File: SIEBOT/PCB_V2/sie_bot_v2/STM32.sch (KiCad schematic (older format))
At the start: 50 parts, among them P11 CONN_3X2, P12 CONN_3X2, P13 CONN_3X2, P14 CONN_3X2, P8 CONN_12X2, P9 CONN_12X2, Q2 BS170F, Q3 BS170F, Q4 BS170F, Q5 BS170F, Q6 BS170F, Q7 BS170F, Q8 BS170F, Q9 BS170F, U10 STM32F105RC, U11 LT1117CST-3.3, U12 ZXMHC3F381N8, U13 ZXMHC3F381N8, U14 ZXMHC3F381N8, U15 ZXMHC3F381N8, X3 8MHz

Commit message: Ruteo de 3 puentes H, se elimina uno por falta de espacio
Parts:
- removed P14: CONN_3X2, pin_array_3x2, symbol CONN_3X2
- removed Q8, Q9: BS170F, BS170F, symbol MOSFET_N_OPENDOUS
- removed R42, R43: 2.2k, SM0603, symbol R
- removed U15: ZXMHC3F381N8, -SO8, symbol ZXMHC3F381N8
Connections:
- net labels removed: C1M4, C2M4, GMTR4, M41, M42, VMTR4
- wire segments 260 -> 236
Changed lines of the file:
@@
-EESchema Schematic File Version 2  date Sun 02 Oct 2011 08:48:42 PM COT
+EESchema Schematic File Version 2  date Mon 03 Oct 2011 08:26:41 AM COT
 LIBS:con-jack
 LIBS:adm3101e
@@
 Comment4 ""
 $EndDescr
-Text Label 10650 8450 0    60   ~ 0
-M42
-Wire Wire Line
-	10600 8550 11000 8550
-Wire Wire Line
-	10600 8450 11000 8450
-Wire Wire Line
-	10600 8350 11000 8350
-Text Label 10650 8550 0    60   ~ 0
-C2M4
-Text Label 10650 8350 0    60   ~ 0
-VMTR4
-Wire Wire Line
-	9450 8350 9800 8350
-Wire Wire Line
-	9450 8450 9800 8450
-Wire Wire Line
-	9450 8550 9800 8550
-Text Label 9450 8550 0    60   ~ 0
-C1M4
-Text Label 9450 8350 0    60   ~ 0
-GMTR4
-Text Label 9450 8450 0    60   ~ 0
-M41
 Text Label 8900 8350 0    60   ~ 0
 VMTR3
@@
 Wire Wire Line
 	7850 6050 8200 6050
-Connection ~ 11100 7650
-Wire Wire Line
-	11100 7650 11100 7350
-Wire Wire Line
-	11100 6650 11100 7050
-Wire Wire Line
-	9550 7050 9400 7050
-Wire Wire Line
-	9400 7050 9400 7950
-Wire Wire Line
-	9400 7950 10150 7950
-Wire Wire Line
-	11100 7350 10950 7350
-Wire Wire Line
-	10050 7650 9650 7650
-Wire Wire Line
-	10150 6350 9500 6350
-Wire Wire Line
-	9550 7350 9500 7350
-Wire Wire Line
-	11100 7050 10950 7050
-Wire Wire Line
-	9000 7150 9550 7150
-Wire Wire Line
-	11350 7150 10950 7150
-Wire Wire Line
-	9000 7250 9550 7250
-Wire Wire Line
-	11200 7250 10950 7250
-Wire Wire Line
-	10050 6650 9650 6650
-Wire Wire Line
-	11350 6650 10450 6650
-Connection ~ 11100 6650
-Wire Wire Line
-	11350 7650 10450 7650
-Wire Wire Line
-	9500 7350 9500 6350
-Connection ~ 11350 7150
 Connection ~ 8850 7150
 Wire Wire Line
@@
 Wire Wire Line
 	7850 5950 8200 5950
-$Comp
-L CONN_3X2 P14
-U 1 1 4E88DB80
-P 10200 8500
-F 0 "P14" H 10200 8750 50  0000 C CNN
-F 1 "CONN_3X2" V 10200 8550 40  0000 C CNN
-F 2 "pin_array_3x2" H 10200 8500 60  0001 C CNN
-	1    10200 8500
-	1    0    0    -1
-$EndComp
 $Comp
 L CONN_3X2 P13
@@
 	1    0    0    -1
 $EndComp
-Text Label 9600 7950 0    60   ~ 0
-C2M4
-Text Label 9600 6350 0    60   ~ 0
-C1M4
 Text Label 7150 6350 0    60   ~ 0
 C1M3
@@
 C1M1
 $Comp
-L ZXMHC3F381N8 U15
-U 1 1 4E87675C
-P 10300 7600
-F 0 "U15" H 10300 7600 60  0000 C CNN
-F 1 "ZXMHC3F381N8" H 10250 8300 60  0000 C CNN
-F 2 "-SO8" H 10300 7600 60  0001 C CNN
-	1    10300 7600
-	1    0    0    -1
-$EndComp
-Text Label 11000 7150 0    60   ~ 0
-VMTR4
-Text Label 9100 7250 0    60   ~ 0
-GMTR4
-Text Label 9100 7150 0    60   ~ 0
-M41
-Text Label 11000 7250 0    60   ~ 0
-M42
-$Comp
-L MOSFET_N_OPENDOUS Q8
-U 1 1 4E87675B
-P 10250 6550
-F 0 "Q8" H 10250 6740 30  0000 R CNN
-F 1 "BS170F" H 10250 6370 30  0000 R CNN
-F 2 "BS170F" H 10250 6550 60  0001 C CNN
-	1    10250 6550
-	0    1    1    0
-$EndComp
-$Comp
-L R R42
-U 1 1 4E87675A
-P 11350 6900
-F 0 "R42" V 11430 6900 50  0000 C CNN
-F 1 "2.2k" V 11350 6900 50  0000 C CNN
-F 2 "SM0603" H 11350 6900 60  0001 C CNN
-	1    11350 6900
-	-1   0    0    1
-$EndComp
-Text Label 9700 6650 0    60   ~ 0
-GMTR4
-Text Label 9700 7650 0    60   ~ 0
-GMTR4
-$Comp
-L R R43
-U 1 1 4E876759
-P 11350 7400
-F 0 "R43" V 11430 7400 50  0000 C CNN
-F 1 "2.2k" V 11350 7400 50  0000 C CNN
-F 2 "SM0603" H 11350 7400 60  0001 C CNN
-	1    11350 7400
-	-1   0    0    -1
-$EndComp
-$Comp
-L MOSFET_N_OPENDOUS Q9
-U 1 1 4E876758
-P 10250 7750
-F 0 "Q9" H 10250 7940 30  0000 R CNN
-F 1 "BS170F" H 10250 7570 30  0000 R CNN
-F 2 "BS170F" H 10250 7750 60  0001 C CNN
-	1    10250 7750
-	0    1    -1   0
-$EndComp
-$Comp
 L MOSFET_N_OPENDOUS Q7

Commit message: Inicio del ruteo de las fuentes de alimentación
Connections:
- net labels added: VDDAST
- wire segments 236 -> 240

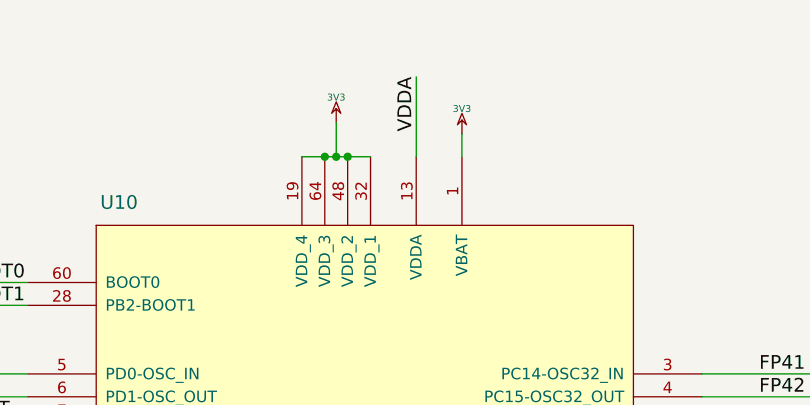
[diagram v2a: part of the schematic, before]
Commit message: Ruteo de la señal de treset del STM, re-asignación de señales de los conectores para facilitar el ruteo
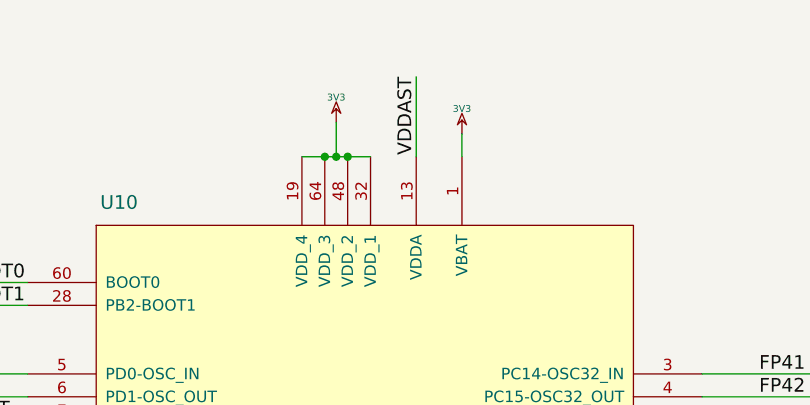
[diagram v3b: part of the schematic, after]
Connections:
- net labels removed: VDDA
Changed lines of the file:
@@
-EESchema Schematic File Version 2  date Mon 03 Oct 2011 02:28:03 PM COT
+EESchema Schematic File Version 2  date Tue 04 Oct 2011 08:25:17 AM COT
 LIBS:con-jack
 LIBS:adm3101e
@@
 Sheet 2 5
 Title ""
-Date "3 oct 2011"
+Date "4 oct 2011"
 Rev ""
 Comp ""
@@
 DECOUPLING
 Text Label 4500 900  3    60   ~ 0
-VDDA
+VDDAST
 Text Label 9800 2300 2    60   ~ 0
 VDDAST

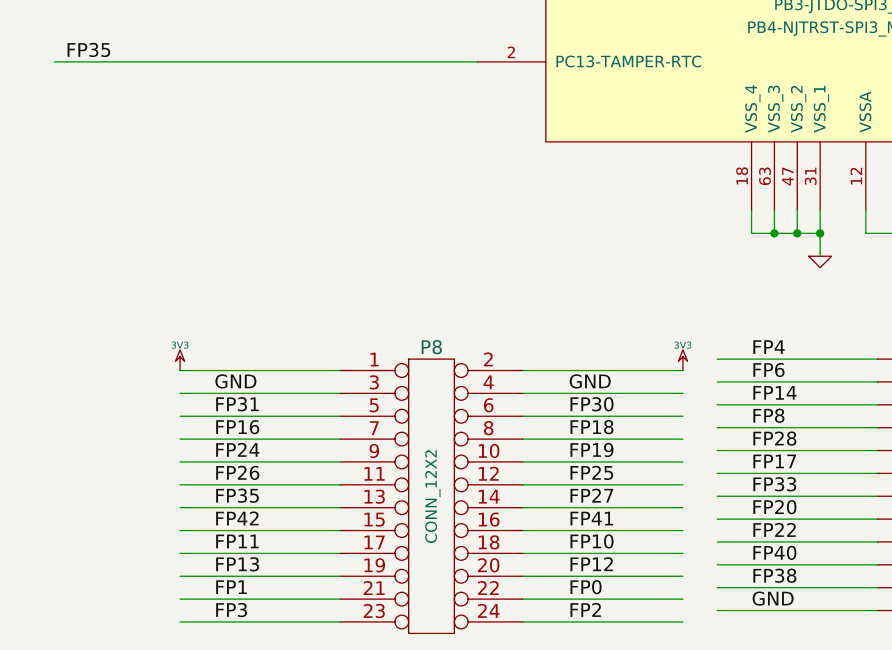
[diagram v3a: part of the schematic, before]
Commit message: Ruteo de todas las señales finalizado. Cambio de JP4 y JP5, ahora se usarán R42 y R43 para conectar las señales del USB host del IMX con el hub, estas resistencias no se soldarán en producción, ya que es necesario cambiar la configuración de los registros OTP para permitir la inicialización por la SD
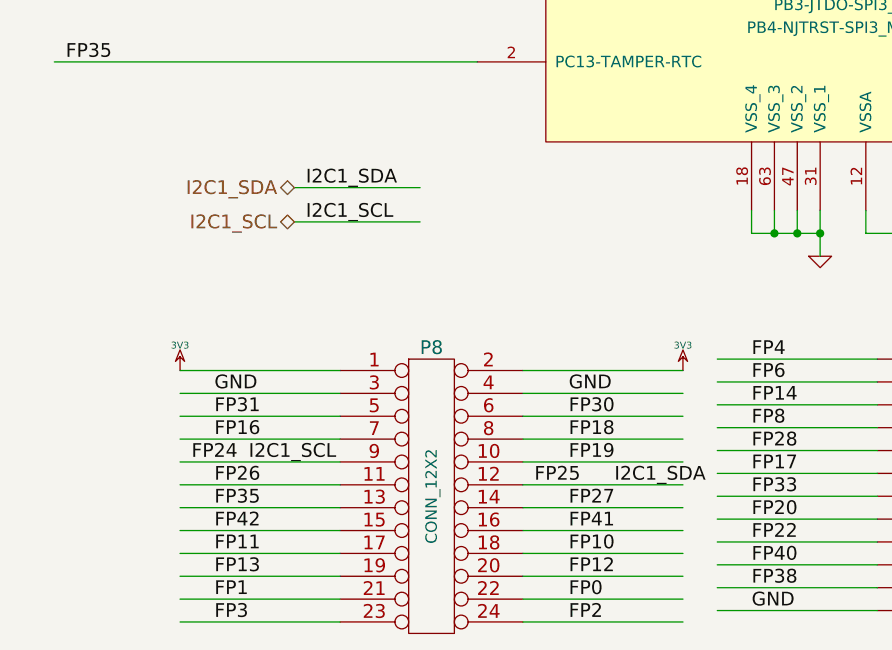
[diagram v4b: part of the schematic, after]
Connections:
- wire segments 240 -> 242

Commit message: Creación de los Gerbers, finalización del ruteo, adición del cuarto puenteH
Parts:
- added P14: CONN_3X2, pin_array_3x2, symbol CONN_3X2
- added Q8, Q9: BS170F, BS170F, symbol MOSFET_N_OPENDOUS
- added R44, R45: 2.2k, SM0603, symbol R
- added U15: ZXMHC3F381N8, -SO8, symbol ZXMHC3F381N8
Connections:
- net labels added: C1M4, C2M4, GMTR4, M41, M42, VMTR4
- wire segments 242 -> 266
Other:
- moved on the sheet: P13, R40, R41, U14
